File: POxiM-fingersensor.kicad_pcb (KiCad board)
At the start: 2 copper layers, 31 x 40 mm, 9 parts, among them J1 To LED board, J2 To photodiode board, J3 To readout unit

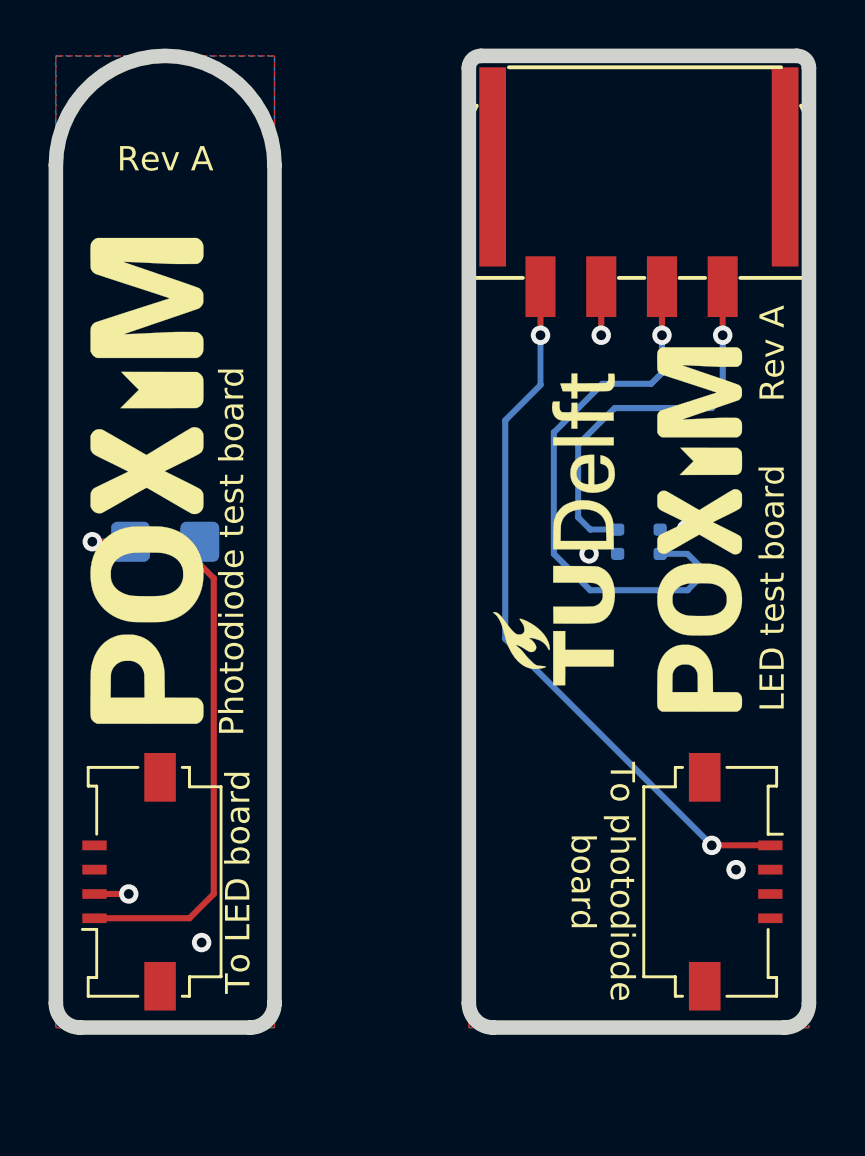
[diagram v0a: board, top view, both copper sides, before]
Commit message: Move to flelex layout
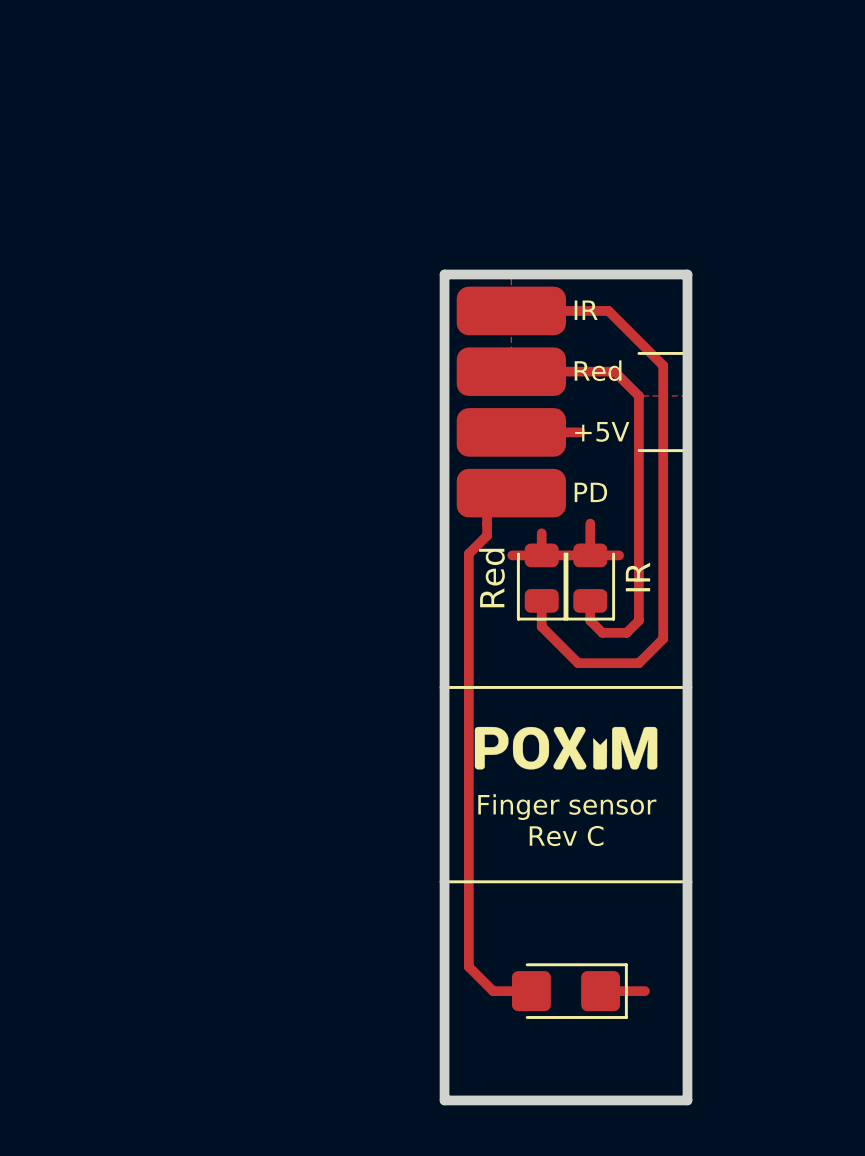
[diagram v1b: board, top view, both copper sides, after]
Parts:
- removed CA1: 50mm FFC, POxiM-uncategorised:Accesory
- removed the G*** at (108.5, 69.5)
- removed the G*** at (114.5, 69.5)
- removed the G*** at (91.8, 67.5)
- removed J1: To LED board, POxiM-uncategorised:Molex_200528-0040_1x04-1MP_P1.00mm_Horizontal
- removed J2: To photodiode board, POxiM-uncategorised:Molex_200528-0040_1x04-1MP_P1.00mm_Horizontal
- added D3: Red (660nm), LED_SMD:LED_0805_2012Metric, F.Cu at (110.0, 71.5)
- added G***: LOGO, POxiM-logos:POxiMLogo_GoldHeart_W7_5mm, F.Cu at (109.0, 78.5)
- D1: moved to F.Cu
- D2: value IR and red -> IR (940nm); footprint POxiM-uncategorised:VSMD66694 -> LED_SMD:LED_0805_2012Metric; moved to F.Cu
- J3: footprint POxiM-uncategorised:Molex-Nanofit-4 -> POxiM-uncategorised:Finger-CableConnection
- moved D1 24.8 mm to (109.0, 88.5), turned to 180 degrees
- moved J3 7.08 mm to (106.8, 64.2)
- moved D2 4.27 mm to (108.0, 71.5), turned to 90 degrees
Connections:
- D1 pad 1: Net-(D1-Pad1) -> +5V
- D1 pad 2: GND -> /Photodiode
- D2 pad 1: GND -> /LED.IR
- D2 pad 2: Net-(D2-Pad2) -> +5V
- J3 pad 1: Net-(J2-Pad1) -> /LED.IR
- J3 pad 2: GND -> /LED.Red
- J3 pad 3: Net-(D2-Pad4) -> +5V
- J3 pad 4: Net-(D2-Pad2) -> /Photodiode
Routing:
- net Net-(J2-Pad1): track 29.5 -> 0.00 mm, vias 2 -> 0
- net /LED.IR: track 0.00 -> 25.5 mm
- net Net-(D1-Pad1): track 25.5 -> 0.00 mm, vias 1 -> 0
- net Net-(D2-Pad4): track 23.2 -> 0.00 mm, vias 1 -> 0
- net /Photodiode: track 0.00 -> 22.5 mm
- net /LED.Red: track 0.00 -> 18.1 mm
- net Net-(D2-Pad2): track 16.1 -> 0.00 mm, vias 1 -> 0
- net +5V: track 0.00 -> 11.3 mm
- net GND: track 3.41 -> 0.00 mm, vias 6 -> 0
- added copper zone on F.Cu, net +5V
- added copper zone on F.Cu, net /LED.IR
- removed copper zone on B.Cu, net GND
- removed copper zone on F.Cu, net GND
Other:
- board size 31 x 40 mm -> 10 x 34 mm
- net class Default: trace_width 0.25 -> 0.2
- board text added: "+5V"
- board text added: "Finger sensor Rev C"
- board text added: "PD"
- board text added: "Red"
- board text removed: "LED test board"
- board text removed: "Photodiode test board"
- board text removed: "RED"
- board text removed: "Rev A"
- board text removed: "To LED board"
- board text removed: "To photodiode board"

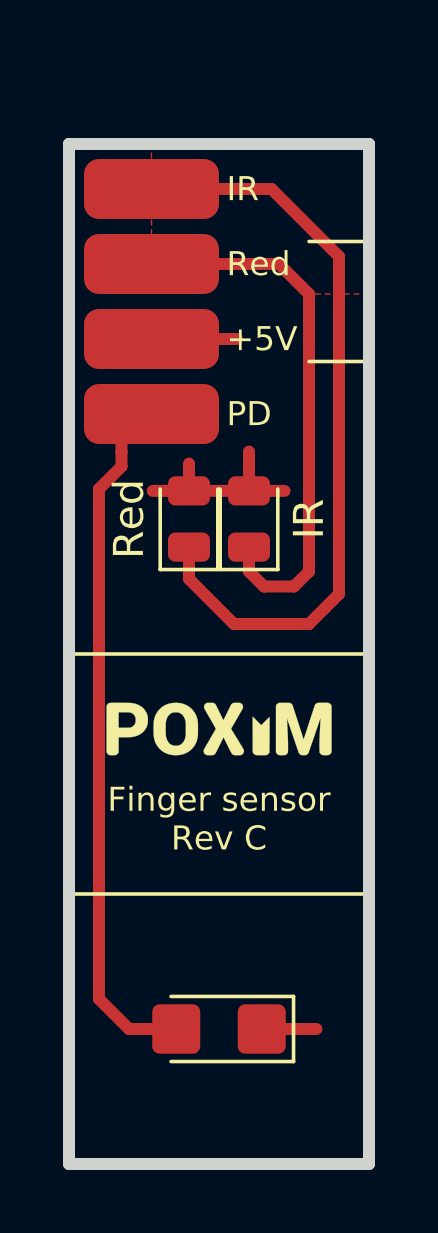
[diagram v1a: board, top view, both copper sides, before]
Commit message: Create rigid option Rev D
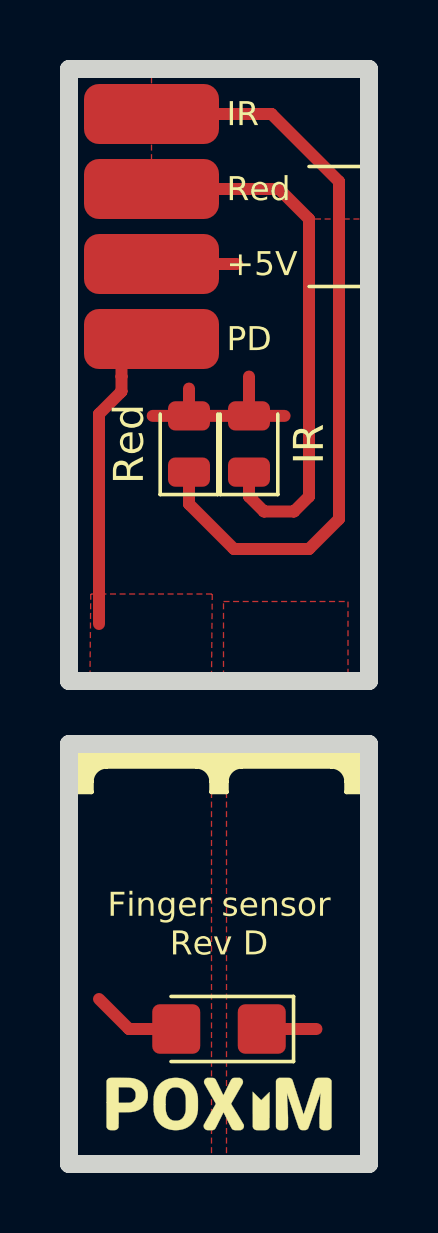
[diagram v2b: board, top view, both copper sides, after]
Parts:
- moved G*** 12.5 mm to (109.0, 91.0)
- moved D2 2.50 mm to (108.0, 69.0)
- moved D3 2.50 mm to (110.0, 69.0)
- moved J3 2.50 mm to (106.8, 61.8)
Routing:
- net /Photodiode: track 22.5 -> 12.5 mm
- added copper zone on F.Cu, net /Photodiode
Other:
- board size 10 x 34 mm -> 10 x 36.5 mm
- board text added: "Finger sensor Rev D"
- board text removed: "Finger sensor Rev C"
